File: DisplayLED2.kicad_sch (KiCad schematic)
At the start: 72 parts

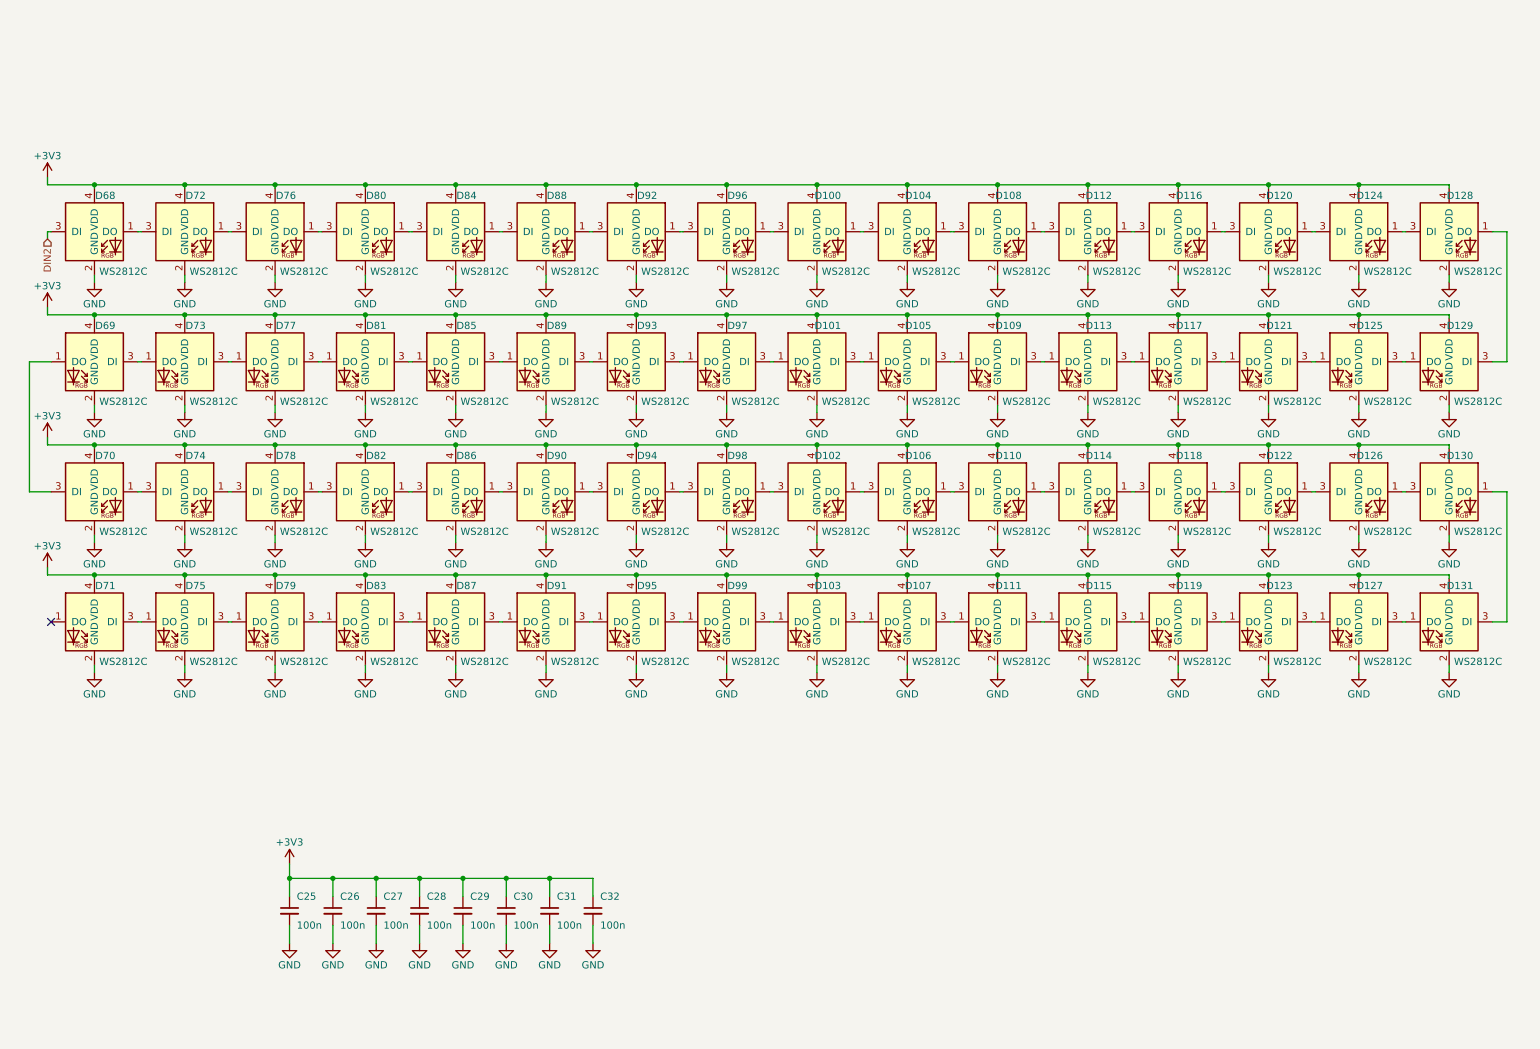
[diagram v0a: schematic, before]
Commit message: Schematic finished, routing PCB started.
Signed-off-by: Ion Bold <bold.ion86@gmail.com>
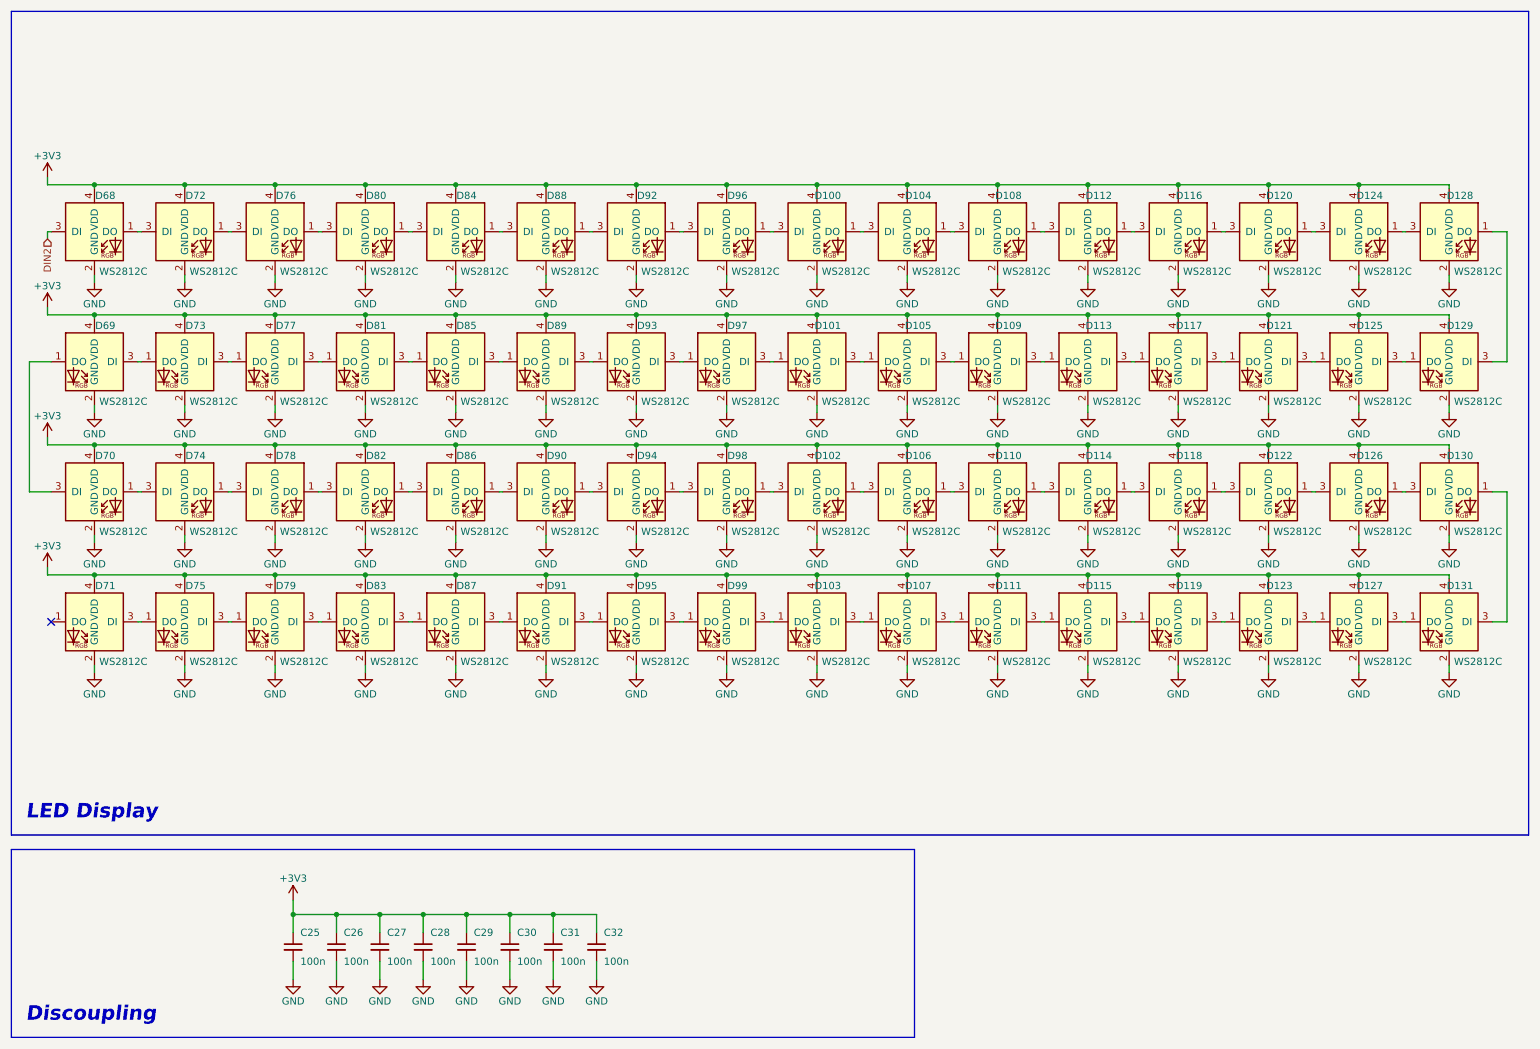
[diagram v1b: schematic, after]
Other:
- note added: "Discoupling"
- note added: "LED Display"
- moved on the sheet: C25, C26, C27, C28, C29, C30, C31, C32
